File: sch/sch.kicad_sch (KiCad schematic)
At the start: 54 parts, among them U2 PCA9548ADB, U3 MPR121QR2_BOARD, U4 MPR121QR2_BOARD, U5 MPR121QR2_BOARD, U6 ProMicro

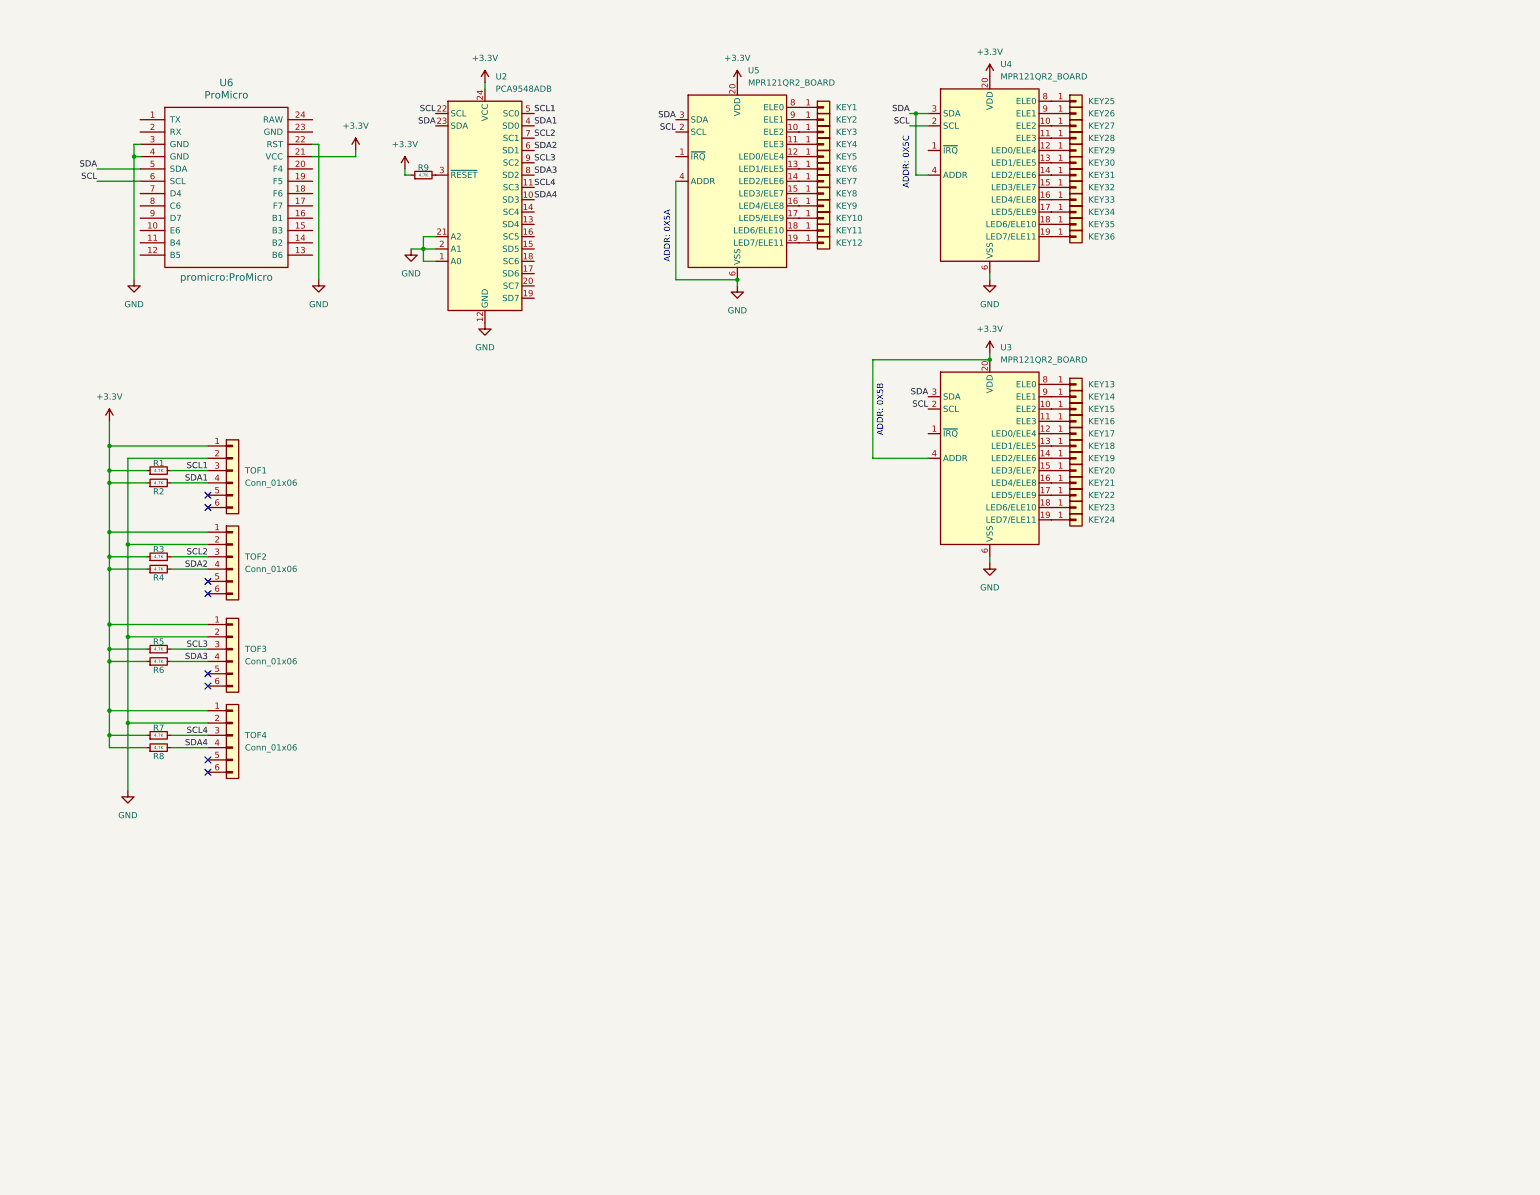
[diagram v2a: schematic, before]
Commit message: Revision 2 of the PCB
Updated to using stm32f4 and a more modular design
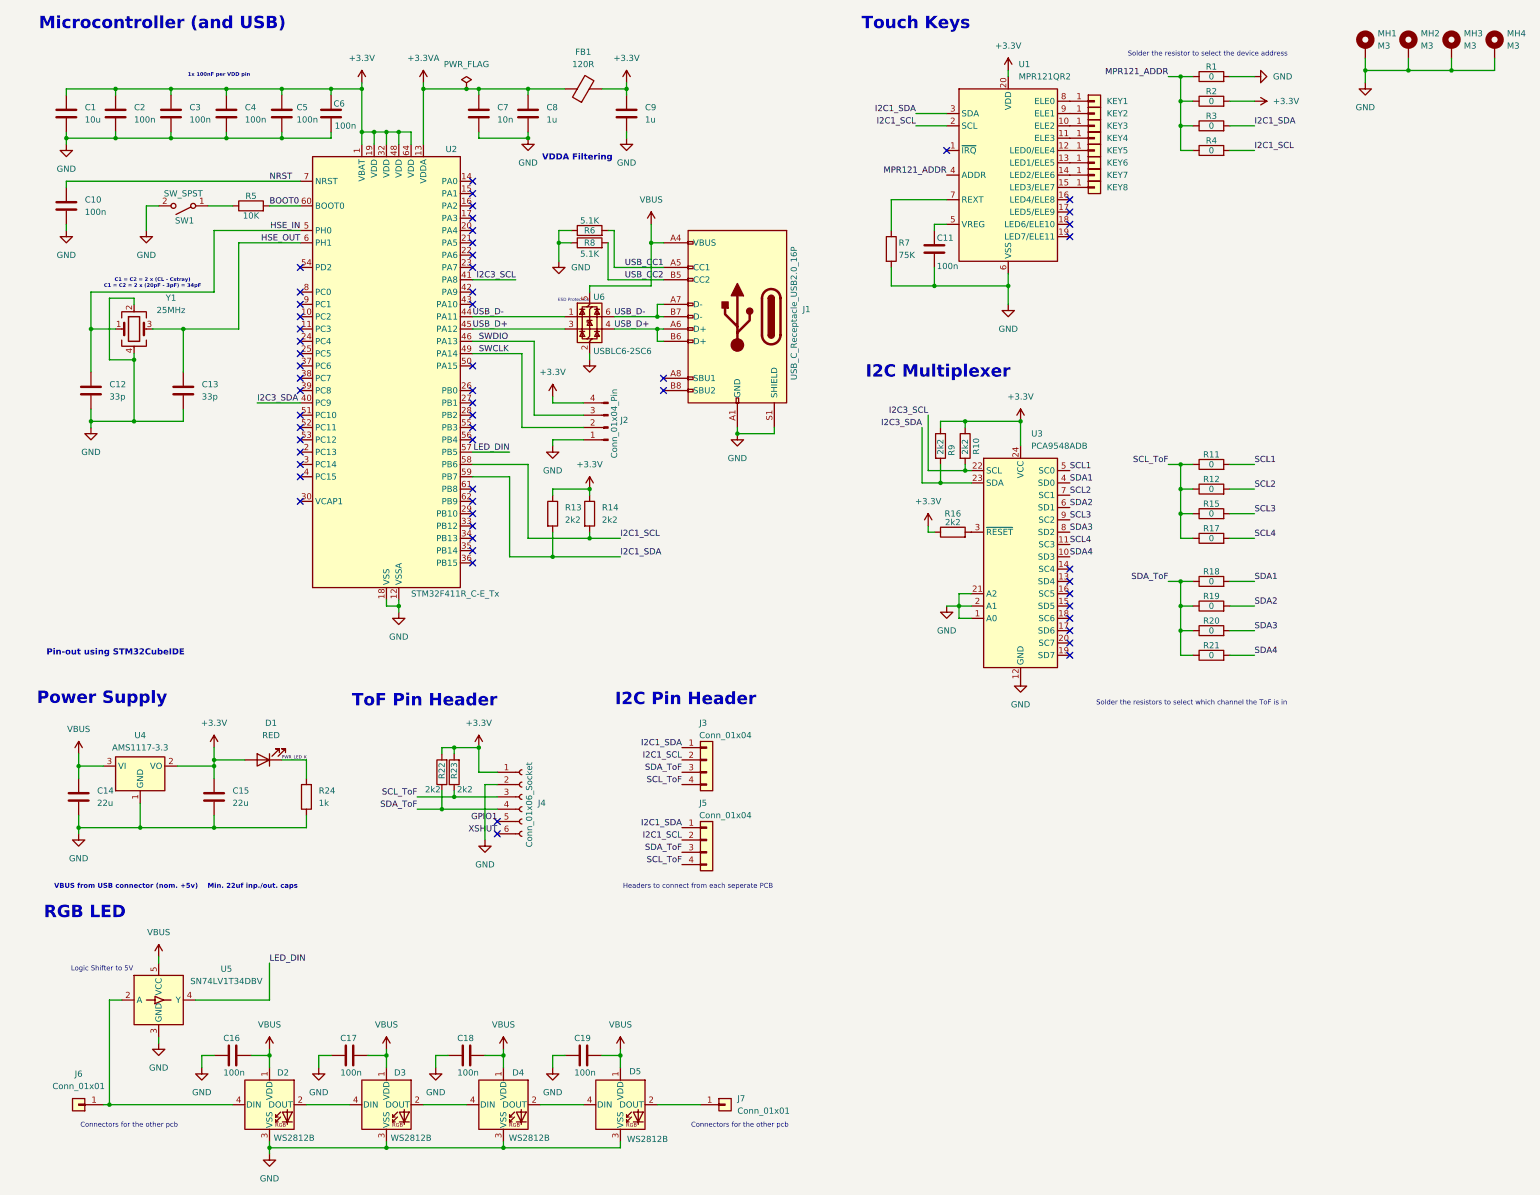
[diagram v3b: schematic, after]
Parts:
- removed KEY10, KEY11, KEY12, KEY13, KEY14, KEY15, KEY16, KEY17, KEY18, KEY19, KEY20, KEY21, KEY22, KEY23, KEY24, KEY25, KEY26, KEY27, KEY28, KEY29, KEY30, KEY31, KEY32, KEY33, KEY34, KEY35, KEY36, KEY9: Conn_01x01, chu_main:ChuKey, symbol Connector_Generic:Conn_01x01
- removed R1, R2, R3, R4, R5, R6, R7, R8, R9: 4.7K, Resistor_SMD:R_0603_1608Metric, symbol Device:R_Small
- removed TOF1, TOF2, TOF3, TOF4: Conn_01x06, Connector_PinSocket_2.54mm:PinSocket_1x06_P2.54mm_Vertical, symbol Connector_Generic:Conn_01x06
- removed U3, U4, U5: MPR121QR2_BOARD, chu_main:MPR121_BOARD, symbol chu_main:MPR121QR2_BOARD
- removed U6: ProMicro, promicro:ProMicro, symbol promicro:ProMicro
- added C1: 10u, Capacitor_SMD:C_0603_1608Metric_Pad1.08x0.95mm_HandSolder, symbol Device:C
- added C10, C11, C16, C17, C18, C19, C2, C3, C4, C5, C6: 100n, Capacitor_SMD:C_0603_1608Metric_Pad1.08x0.95mm_HandSolder, symbol Device:C
- added C12, C13: 33p, Capacitor_SMD:C_0603_1608Metric_Pad1.08x0.95mm_HandSolder, symbol Device:C
- added C14, C15: 22u, Capacitor_SMD:C_0805_2012Metric, symbol Device:C
- added C7: 10n, Capacitor_SMD:C_0603_1608Metric_Pad1.08x0.95mm_HandSolder, symbol Device:C
- added C8, C9: 1u, Capacitor_SMD:C_0603_1608Metric_Pad1.08x0.95mm_HandSolder, symbol Device:C
- added D1: RED, LED_SMD:LED_0201_0603Metric, symbol Device:LED
- added D2, D3, D4, D5: WS2812B, LED_SMD:LED_WS2812B_PLCC4_5.0x5.0mm_P3.2mm, symbol LED:WS2812B
- added FB1: 120R, Inductor_SMD:L_0603_1608Metric, symbol Device:FerriteBead
- added J1: USB_C_Receptacle_USB2.0_16P, Connector_USB:USB_C_Receptacle_GCT_USB4105-xx-A_16P_TopMnt_Horizontal, symbol Connector:USB_C_Receptacle_USB2.0_16P
- added J2: Conn_01x04_Pin, Connector_PinHeader_2.54mm:PinHeader_1x04_P2.54mm_Vertical, symbol Connector:Conn_01x04_Pin
- added J3, J5: Conn_01x04, chu_main:Conn_Solder_I2C, symbol Connector_Generic:Conn_01x04
- added J4: Conn_01x06_Socket, Connector_PinHeader_2.54mm:PinHeader_1x06_P2.54mm_Vertical, symbol Connector:Conn_01x06_Socket
- added J6, J7: Conn_01x01, chu_main:Solder_3P, symbol Connector_Generic:Conn_01x01
- added MH1, MH2, MH3, MH4: M3, MountingHole:MountingHole_3.2mm_M3_Pad_Via, symbol Mechanical:MountingHole_Pad
- added R1, R11, R12, R15, R17, R18, R19, R2, R20, R21, R3, R4: 0, Resistor_SMD:R_0603_1608Metric_Pad0.98x0.95mm_HandSolder, symbol Device:R
- added R10, R13, R14, R16, R22, R23, R9: 2k2, Resistor_SMD:R_0603_1608Metric_Pad0.98x0.95mm_HandSolder, symbol Device:R
- added R24: 1k, Resistor_SMD:R_0603_1608Metric_Pad0.98x0.95mm_HandSolder, symbol Device:R
- added R5: 10K, Resistor_SMD:R_0603_1608Metric_Pad0.98x0.95mm_HandSolder, symbol Device:R
- added R6, R8: 5.1K, Resistor_SMD:R_0603_1608Metric_Pad0.98x0.95mm_HandSolder, symbol Device:R
- added R7: 75K, Resistor_SMD:R_0603_1608Metric_Pad0.98x0.95mm_HandSolder, symbol Device:R
- added SW1: SW_SPST, Button_Switch_SMD:SW_SPST_TS-1088-xR025, symbol Switch:SW_SPST
- added U1: MPR121QR2, Package_DFN_QFN:UQFN-20_3x3mm_P0.4mm, symbol Sensor_Touch:MPR121QR2
- added U2: STM32F411R_C-E_Tx, Package_QFP:LQFP-64_10x10mm_P0.5mm, symbol MCU_ST_STM32F4:STM32F411R_C-E_Tx
- added U4: AMS1117-3.3, Package_TO_SOT_SMD:SOT-223-3_TabPin2, symbol Regulator_Linear:AMS1117-3.3
- added U5: SN74LV1T34DBV, Package_TO_SOT_SMD:SOT-23-5, symbol Logic_LevelTranslator:SN74LV1T34DBV
- added U6: USBLC6-2SC6, Package_TO_SOT_SMD:SOT-23-6, symbol Power_Protection:USBLC6-2SC6
- added Y1: 25MHz, Crystal:Crystal_SMD_3225-4Pin_3.2x2.5mm_HandSoldering, symbol Device:Crystal_GND24
- renumbered U2 to U3
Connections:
- net +3.3V: now also C1.1, C15.1, C2.1, C3.1, C4.1, C5.1, C6.1, C9.1, D1.2 (A), FB1.2, J2.4 (Pin_4), J4.1 (Pin_1), R10.1, R13.1, R14.1, R16.1, R2.2, R22.2, R23.2, R9.1, U1.20 (VDD), U2.1 (VBAT), U2.19 (VDD), U2.32 (VDD), U2.48 (VDD), U2.64 (VDD), U4.2 (VO)
- net GND: now also C1.2, C10.2, C11.2, C12.2, C13.2, C14.2, C15.2, C16.1, C17.1, C18.1, C19.1, C2.2, C3.2, C4.2, C5.2, C6.2, C7.2, C8.2, C9.2, D2.3 (VSS), D3.3 (VSS), D4.3 (VSS), D5.3 (VSS), J1.A1 (GND), J1.A12 (GND), J1.B1 (GND), J1.B12 (GND), J1.S1 (SHIELD), J2.1 (Pin_1), J4.2 (Pin_2), MH1.1, MH2.1, MH3.1, MH4.1, R1.2, R24.1, R6.1, R7.2, R8.1, SW1.2 (B), U1.6 (VSS), U2.12 (VSSA), U2.18 (VSS), U2.31 (VSS), U2.47 (VSS), U2.63 (VSS), U4.1 (GND), U5.3 (GND), U6.2 (GND), Y1.2, Y1.4
- net SCL1: now also R11.2
- net SCL2: now also R12.2
- net SCL3: now also R15.2
- net SCL4: now also R17.2
- net SDA1: now also R18.2
- net SDA2: now also R19.2
- net SDA3: now also R20.2
- net SDA4: now also R21.2
- net at KEY4.1 (Pin_1): now also U1.11 (ELE3)
- net at U3.3 (~{RESET}): now also R16.2
- net at KEY5.1 (Pin_1): now also U1.12 (LED0/ELE4)
- net at KEY6.1 (Pin_1): now also U1.13 (LED1/ELE5)
- net at KEY3.1 (Pin_1): now also U1.10 (ELE2)
- net at KEY2.1 (Pin_1): now also U1.9 (ELE1)
- net at KEY7.1 (Pin_1): now also U1.14 (LED2/ELE6)
- net at KEY8.1 (Pin_1): now also U1.15 (LED3/ELE7)
- net at KEY1.1 (Pin_1): now also U1.8 (ELE0)
- net SCL renamed I2C3_SCL
- net I2C3_SCL: now also R10.2, U2.41 (PA8)
- net SDA renamed I2C3_SDA
- net I2C3_SDA: now also R9.2, U2.40 (PC9)
- new net: R5.1, SW1.1 (A)
- new net: D4.2 (DOUT), D5.4 (DIN)
- new net: D3.2 (DOUT), D4.4 (DIN)
- new net: D2.4 (DIN), J6.1 (Pin_1), U5.2 (A)
- new net: D5.2 (DOUT), J7.1 (Pin_1)
- new net: R7.1, U1.7 (REXT)
- new net: C11.1, U1.5 (VREG)
- new net: D2.2 (DOUT), D3.4 (DIN)
- new net +3.3VA: C7.1, C8.1, FB1.1, U2.13 (VDDA)
- new net BOOT0: R5.2, U2.60 (BOOT0)
- new net GPIO1: J4.5 (Pin_5)
- new net HSE_IN: C12.1, U2.5 (PH0), Y1.1
- new net HSE_OUT: C13.1, U2.6 (PH1), Y1.3
- new net I2C1_SCL: J3.2 (Pin_2), J5.2 (Pin_2), R14.2, R4.2, U1.2 (SCL), U2.58 (PB6)
- new net I2C1_SDA: J3.1 (Pin_1), J5.1 (Pin_1), R13.2, R3.2, U1.3 (SDA), U2.59 (PB7)
- new net LED_DIN: U2.57 (PB5), U5.4 (Y)
- new net MPR121_ADDR: R1.1, R2.1, R3.1, R4.1, U1.4 (ADDR)
- new net NRST: C10.1, U2.7 (NRST)
- new net PWR_LED_K: D1.1 (K), R24.2
- new net SCL_ToF: J3.4 (Pin_4), J4.3 (Pin_3), J5.4 (Pin_4), R11.1, R12.1, R15.1, R17.1, R23.1
- new net SDA_ToF: J3.3 (Pin_3), J4.4 (Pin_4), J5.3 (Pin_3), R18.1, R19.1, R20.1, R21.1, R22.1
- new net SWCLK: J2.2 (Pin_2), U2.49 (PA14)
- new net SWDIO: J2.3 (Pin_3), U2.46 (PA13)
- new net USB_CC1: J1.A5 (CC1), R6.2
- new net USB_CC2: J1.B5 (CC2), R8.2
- new net USB_D+: J1.A6 (D+), J1.B6 (D+), U2.45 (PA12), U6.3 (I/O2), U6.4 (I/O2)
- new net USB_D-: J1.A7 (D-), J1.B7 (D-), U2.44 (PA11), U6.1 (I/O1), U6.6 (I/O1)
- new net VBUS: C14.1, C16.2, C17.2, C18.2, C19.2, D2.1 (VDD), D3.1 (VDD), D4.1 (VDD), D5.1 (VDD), J1.A4 (VBUS), J1.A9 (VBUS), J1.B4 (VBUS), J1.B9 (VBUS), U4.3 (VI), U5.5 (VCC), U6.5 (VBUS)
- new net XSHUT: J4.6 (Pin_6)
- no-connect marks 8 -> 57
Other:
- note added: "1x 100nF per VDD pin"
- note added: "C1 = C2 = 2 x (CL - Cstray) C1 = C2 = 2 x (20pF - 3pF) = 34pF"
- note added: "Connectors for the other pcb"
- note added: "ESD Protection"
- note added: "Headers to connect from each seperate PCB"
- note added: "I2C Multiplexer"
- note added: "I2C Pin Header"
- note added: "Logic Shifter to 5V"
- note added: "Microcontroller (and USB)"
- note added: "Pin-out using STM32CubeIDE"
- note added: "Power Supply"
- note added: "RGB LED"
- note added: "Solder the resistor to select the device address"
- note added: "Solder the resistors to select which channel the ToF is in"
- note added: "ToF Pin Header"
- note added: "Touch Keys"
- note added: "VBUS from USB connector (nom. +5v) Min. 22uf inp./out. caps"
- note added: "VDDA Filtering"
- note removed: "ADDR: 0X5A"
- note removed: "ADDR: 0X5B"
- note removed: "ADDR: 0X5C"
- company: (none) -> Leo_Beo
- title: (none) -> Chunithm_Luminas
- moved on the sheet: KEY1, KEY2, KEY3, KEY4, KEY5, KEY6, KEY7, KEY8, U3

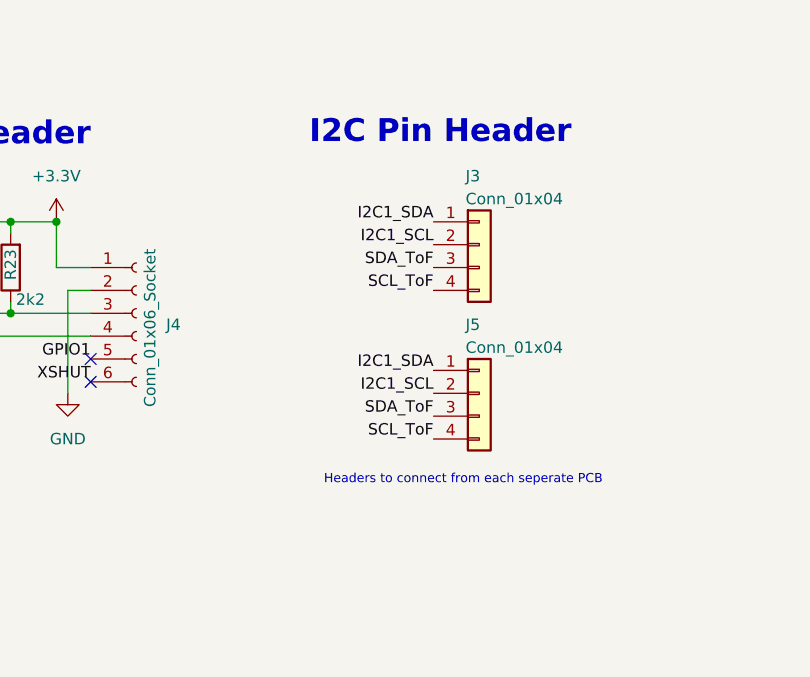
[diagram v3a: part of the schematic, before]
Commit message: Updated side pads with power and ground
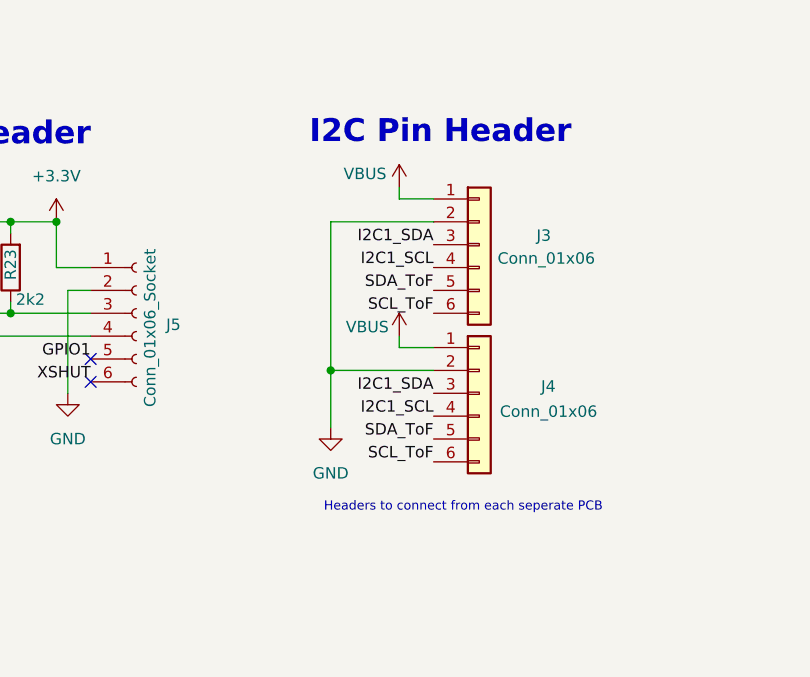
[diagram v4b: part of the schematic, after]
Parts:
- J3: value Conn_01x04 -> Conn_01x06; symbol Connector_Generic:Conn_01x04 -> Connector_Generic:Conn_01x06
- J4: renamed from J5; value Conn_01x04 -> Conn_01x06; symbol Connector_Generic:Conn_01x04 -> Connector_Generic:Conn_01x06
- renumbered J4 to J5
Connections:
- net GND: now also J3.2 (Pin_2), J4.2 (Pin_2)
- net I2C1_SCL: now also J3.4 (Pin_4), J4.4 (Pin_4); no longer J3.2 (Pin_2), J4.2 (Pin_2)
- net I2C1_SDA: now also J3.3 (Pin_3), J4.3 (Pin_3); no longer J3.1 (Pin_1), J4.1 (Pin_1)
- net SCL_ToF: now also J3.6 (Pin_6), J4.6 (Pin_6); no longer J3.4 (Pin_4), J4.4 (Pin_4)
- net SDA_ToF: now also J3.5 (Pin_5), J4.5 (Pin_5); no longer J3.3 (Pin_3), J4.3 (Pin_3)
- net VBUS: now also J3.1 (Pin_1), J4.1 (Pin_1)
